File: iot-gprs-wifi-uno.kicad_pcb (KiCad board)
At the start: 2 copper layers, 110 x 53.3 mm, 73 parts, among them CON1 BARREL_JACK, P1 CAMERASOCKET, P2 CONN_01X12, P3 CONN_01X12, SW1 SW_DIP_x01, U1 usb_mini_b, U2 MCP16311-MNY, U3 CH340G, U4 A20Module, U5 MCP6001R, U6 IRLM6402, U7 BD00GA5WEFJ, U8 SIM, X1 CRYSTAL_ABM3C

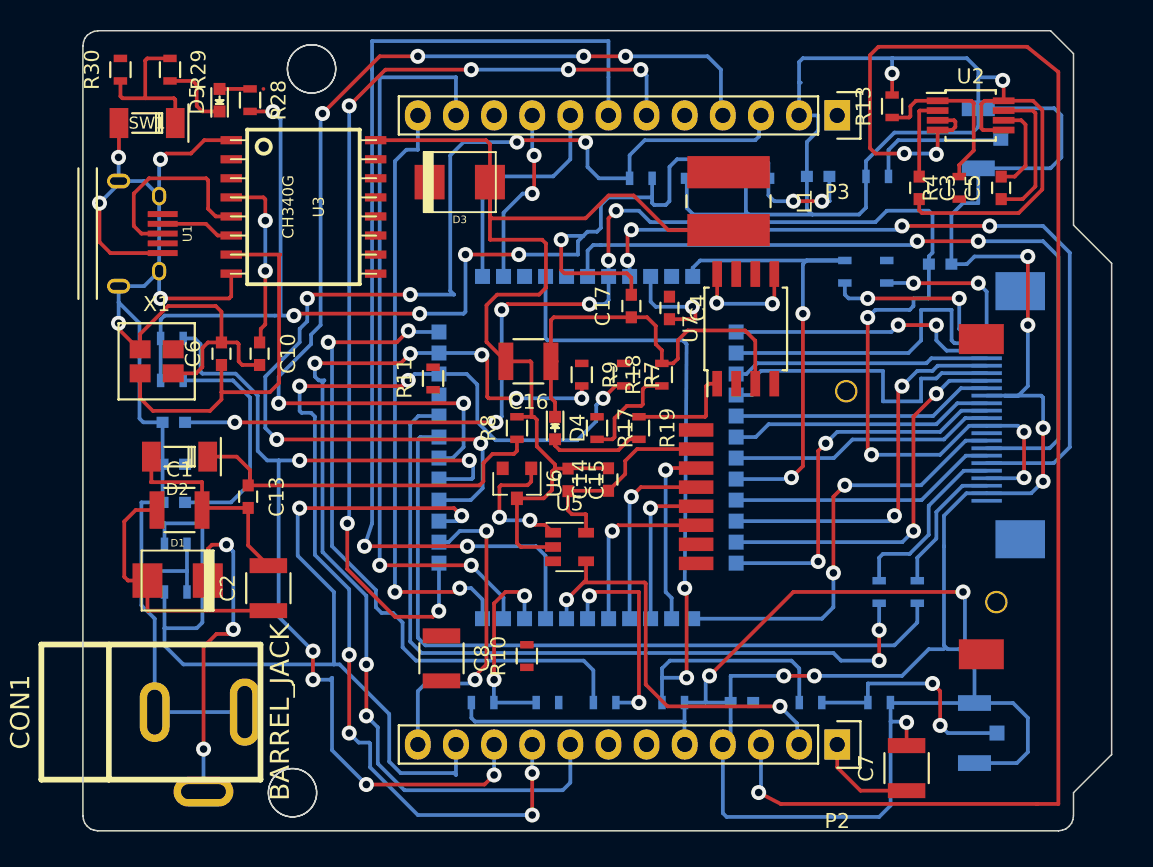
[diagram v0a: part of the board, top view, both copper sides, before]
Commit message: add .gitignore file add fp-lib-table
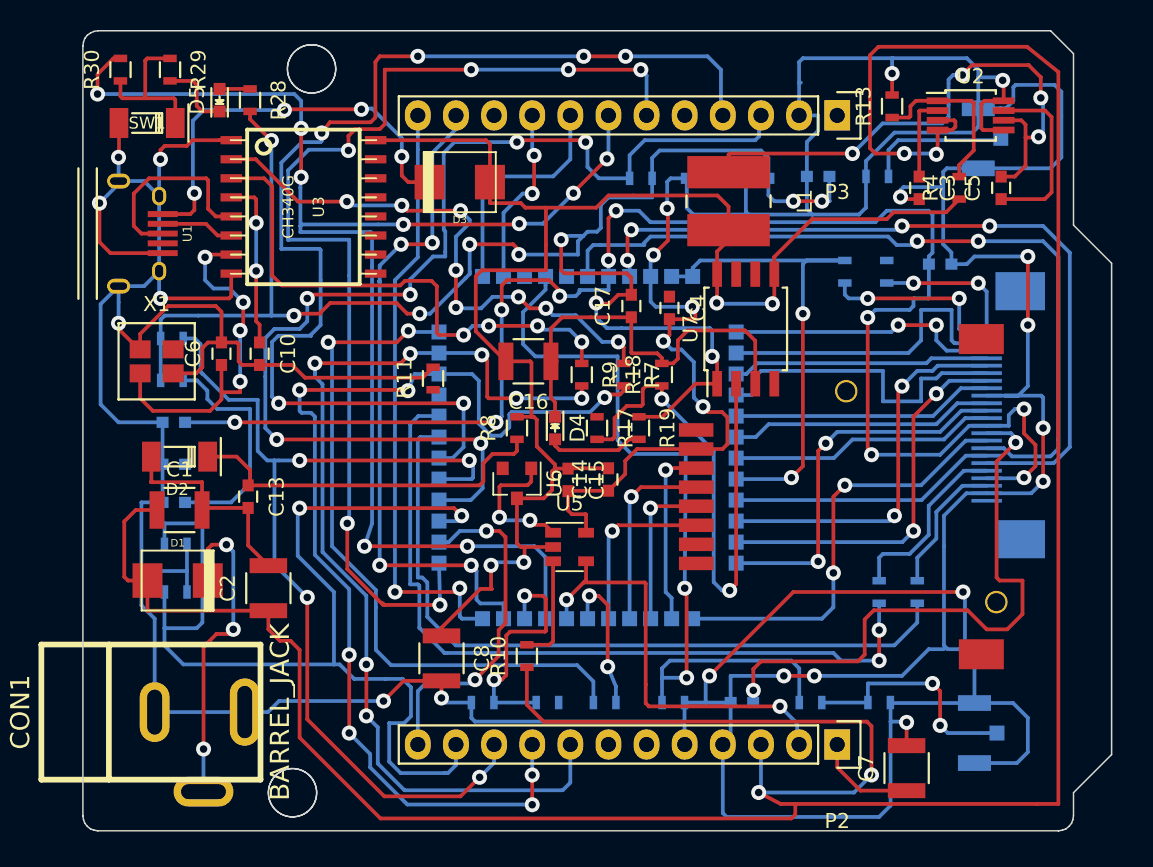
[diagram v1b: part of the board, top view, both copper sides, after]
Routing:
- net Vin: track 118.7 -> 201.8 mm, vias 3 -> 4
- net XO: track 401.5 -> 446.7 mm, vias 17 -> 24
- net VDD_1V8: track 0.00 -> 40.0 mm, vias 0 -> 2
- net Net-(R7-Pad1): track 0.00 -> 37.8 mm, vias 0 -> 8
- net Net-(R9-Pad1): track 0.00 -> 35.4 mm, vias 0 -> 4
- net Net-(C5-Pad2): track 6.24 -> 37.5 mm, vias 0 -> 4
- net Net-(R17-Pad2): track 7.13 -> 36.9 mm, vias 0 -> 2
- net VCC_USB: track 0.00 -> 27.8 mm, vias 0 -> 4
- net VCC5.0: track 87.5 -> 111.7 mm, vias 2 -> 4
- net WIFI_RST: track 71.0 -> 93.2 mm, vias 2 -> 9
- net VCC3.3: track 124.0 -> 137.3 mm, vias 10 -> 12
- net WIFI_IO12: track 65.3 -> 73.2 mm
- net WIFI_IO4: track 69.3 -> 76.8 mm
- net Net-(R10-Pad2): track 0.00 -> 7.17 mm
- net WIFI_TXD: track 50.7 -> 44.8 mm, vias 2 -> 4
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
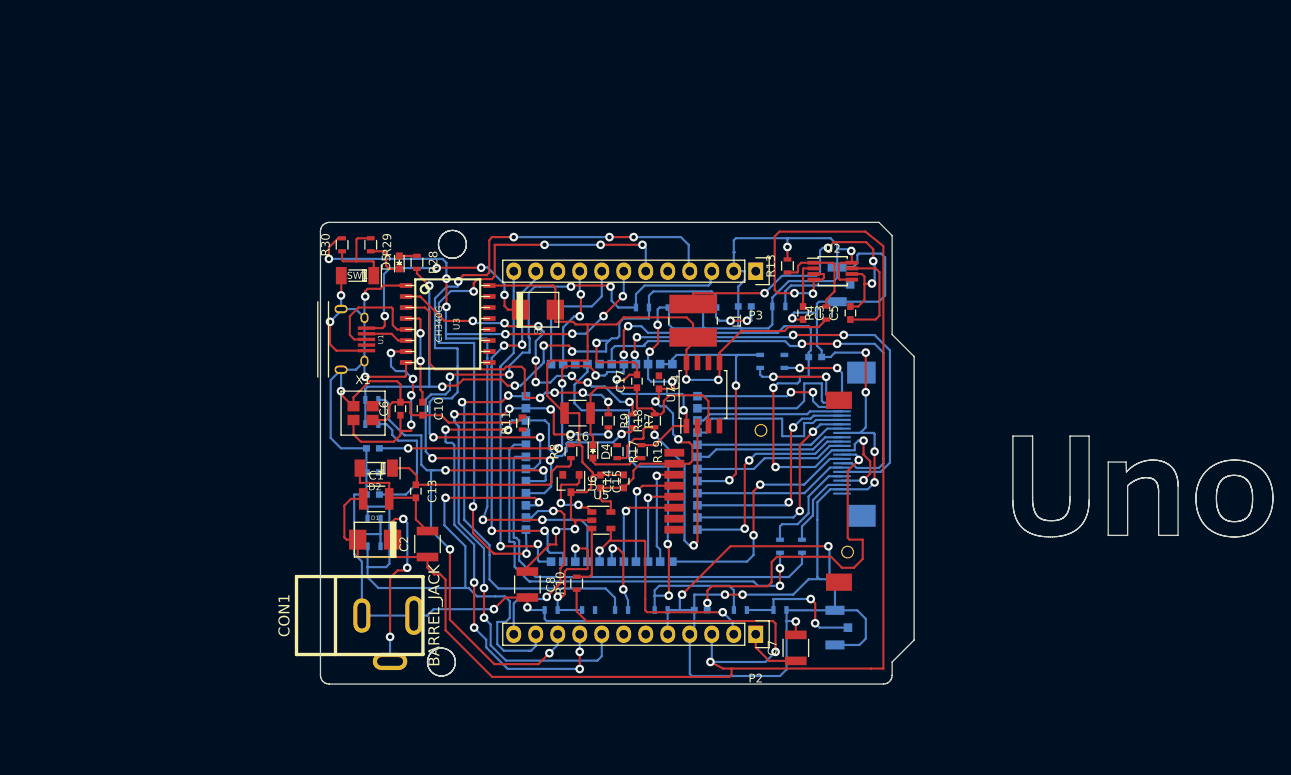
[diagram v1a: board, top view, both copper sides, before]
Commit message: update Kicad PCb iot-gprs-wifi-uno-hw
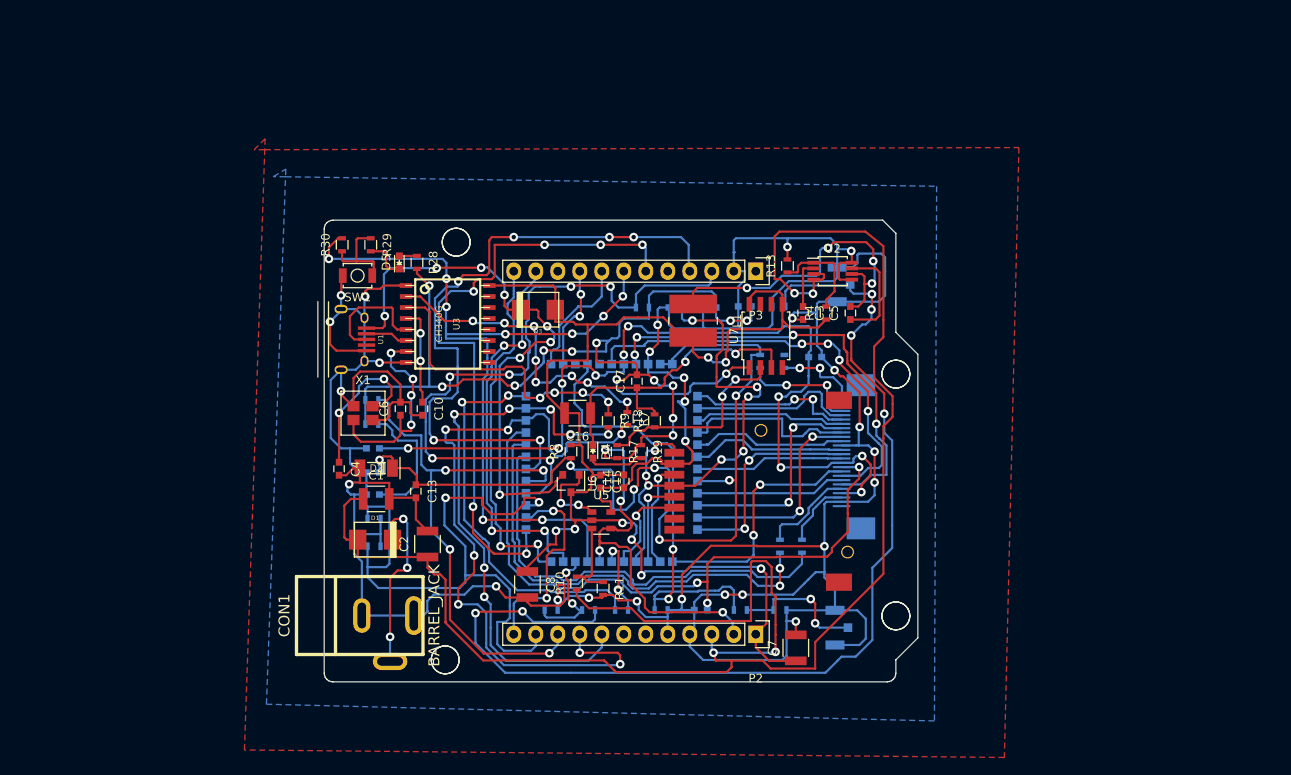
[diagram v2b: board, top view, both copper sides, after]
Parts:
- CON1: footprint A20md:dc_socket -> Footprint:dc_socket
- D1, D3: footprint A20md:do214aa -> Footprint:do214aa
- D2: footprint A20md:SOD-80 -> Footprint:SOD-80
- P1: footprint A20md:camera_socket24aaa -> Footprint:camera_socket24aaa
- SMA1, SMA2: footprint A20md:ANTEN_FP -> Footprint:ANTEN_FP
- SW1: value SW_DIP_x01 -> SW_PUSH; footprint A20md:SOD-80 -> Buttons_Switches_SMD:SW_SPST_B3U-1000P
- U1: footprint A20md:USB_Micro-B -> Footprint:USB_Micro-B
- U3: footprint A20md:soic-16 -> Footprint:soic-16
- U4: footprint A20md:a20module -> Footprint:a20module
- U8: footprint A20md:SIM_HOLD_115A-ADA0-R02 -> Footprint:SIM_HOLD_115A-ADA0-R02
- X1: footprint A20md:Crystal_SMD_3225_12MHz -> Footprint:Crystal_SMD_3225_12MHz
- moved C4 38.3 mm to (127.2, 114.5)
- moved R11 21.2 mm to (157.6, 128.3), turned to 270 degrees
- moved U7 9.92 mm to (176.4, 99.2)
- moved P1 1.45 mm to (188.4, 112.1)
- moved R7 0.66 mm to (160.4, 108.7)
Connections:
- R1 pad 1: XO -> Net-(R1-Pad1)
- R1 pad 2: Net-(R1-Pad2) -> XO
- R17 pad 1: VCC3.3 -> Net-(R17-Pad1)
- R17 pad 2: Net-(R17-Pad2) -> VCC3.3
- R18 pad 1: Net-(R17-Pad2) -> Net-(R17-Pad1)
- R2 pad 2: Net-(R1-Pad2) -> Net-(R1-Pad1)
- U4 pad 21: Net-(R1-Pad2) -> Net-(R1-Pad1)
- U7 pad 2: Net-(R17-Pad2) -> Net-(R17-Pad1)
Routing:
- net Net-(R2-Pad1): track 9.57 -> 124.9 mm, vias 0 -> 6
- net VCC3.9: track 58.3 -> 107.9 mm, vias 2 -> 7
- net VSIM: track 12.8 -> 58.9 mm, vias 1 -> 8
- net VCC5.0: track 111.7 -> 150.5 mm, vias 4 -> 8
- net VCC_USB: track 27.8 -> 64.7 mm, vias 4 -> 8
- net Net-(R17-Pad2): track 36.9 -> 0.00 mm, vias 2 -> 0
- net VDD_1V8: track 40.0 -> 75.8 mm, vias 2 -> 3
- net VCC3.3: track 137.3 -> 171.8 mm, vias 12 -> 18
- net Net-(R17-Pad1): track 0.00 -> 23.5 mm, vias 0 -> 2
- net Net-(C4-Pad1): track 0.00 -> 17.9 mm, vias 0 -> 2
- net Net-(R1-Pad2): track 15.9 -> 0.00 mm, vias 2 -> 0
- net Net-(R1-Pad1): track 0.00 -> 12.7 mm, vias 0 -> 2
- net UART_RXD: track 71.1 -> 83.1 mm
- net XO: track 446.7 -> 436.2 mm, vias 24 -> 27
- net Net-(C16-Pad1): track 28.0 -> 37.5 mm, vias 0 -> 2
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- added copper zone on B.Cu, net XO
- added copper zone on F.Cu, net XO
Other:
- board size 110 x 53.3 mm -> 68.5 x 53.3 mm

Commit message: update schematic iot-gprs-wifi-uno-hw add a20 pretty folder
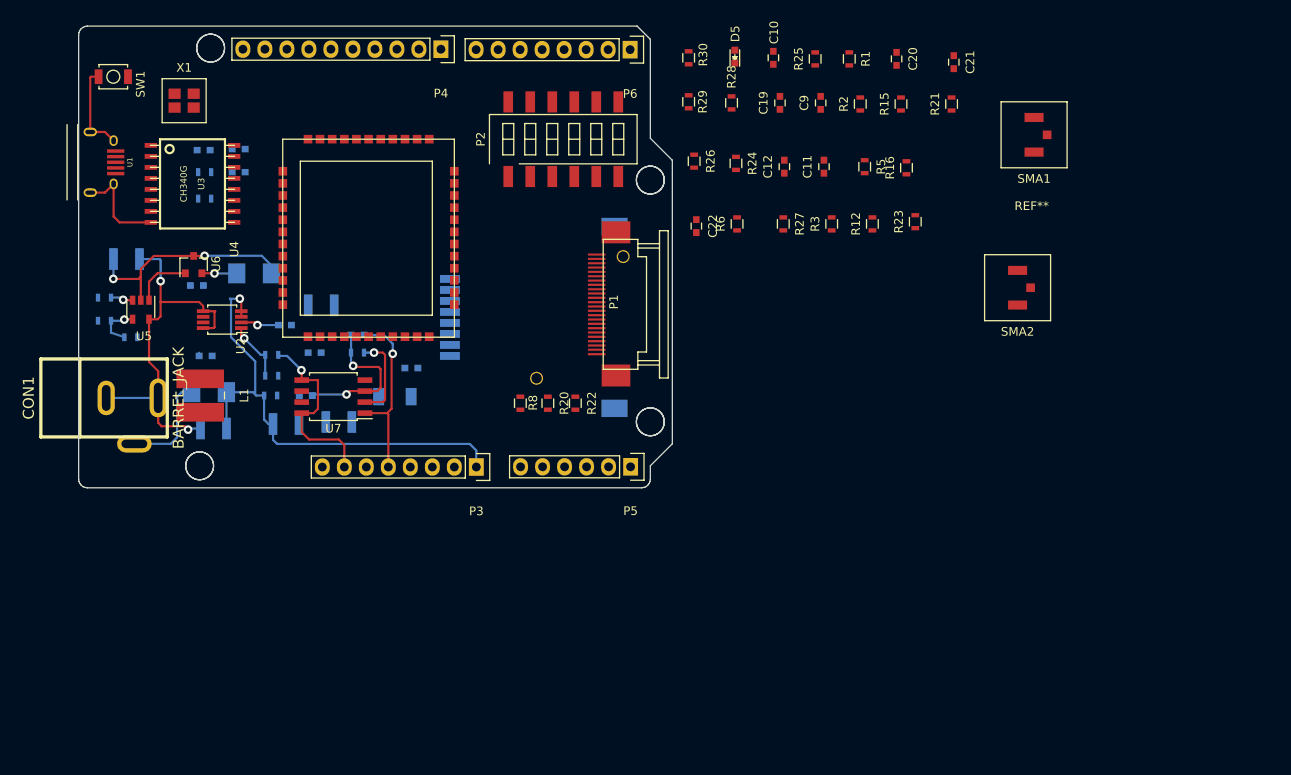
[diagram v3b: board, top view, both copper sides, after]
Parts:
- added Arduino_Header: Val**, A20:arduino_header, B.Cu at (68.2, 158.9)
- added P4: CONN_01X10, Socket_Strips:Socket_Strip_Straight_1x10, F.Cu at (138.9, 66.1)
- added P5: CONN_01X06, Socket_Strips:Socket_Strip_Straight_1x06, F.Cu at (160.8, 114.3)
- added P6: CONN_01X08, Socket_Strips:Socket_Strip_Straight_1x08, F.Cu at (160.8, 66.1)
- added REF**: esp8266.vn, A20:logo-esp8266.vn, F.Cu at (207.1, 83.7)
- C1, C13, C14, C15, C16, C17, C2, C3, C4, C5, C6, C7, C8, D4, R10, R11, R13, R17, R18, R19, R4, R7, R9: moved to B.Cu
- C11, C12, C19, C20, C21, C22, C9, R1, R12, R15, R16, R2, R20, R21, R22, R23, R24, R25, R26, R27, R3, R5, R6: moved to F.Cu
- CON1: footprint Footprint:dc_socket -> A20:dc_socket
- D1, D3: footprint Footprint:do214aa -> A20:do214aa; moved to B.Cu
- D2: footprint Footprint:SOD-80 -> A20:SOD-80; moved to B.Cu
- P1: footprint Footprint:camera_socket24aaa -> A20:camera_socket24aaa; moved to F.Cu
- P2: value CONN_01X12 -> SW2x6; footprint Socket_Strips:Socket_Strip_Straight_1x12 -> Buttons_Switches_ThroughHole:SW_DIP_x6_W8.61mm_Slide_SMD_LowProfile
- P3: value CONN_01X12 -> CONN_01X08; footprint Socket_Strips:Socket_Strip_Straight_1x12 -> Socket_Strips:Socket_Strip_Straight_1x08
- SMA1, SMA2: footprint Footprint:ANTEN_FP -> A20:ANTEN_FP; moved to F.Cu
- U1: footprint Footprint:USB_Micro-B -> A20:USB_Micro-B
- U3: footprint Footprint:soic-16 -> A20:soic-16
- U4: footprint Footprint:a20module -> A20:a20module; moved to F.Cu
- U8: footprint Footprint:SIM_HOLD_115A-ADA0-R02 -> A20:SIM_HOLD_115A-ADA0-R02; moved to B.Cu
- X1: footprint Footprint:Crystal_SMD_3225_12MHz -> A20:Crystal_SMD_3225_12MHz
- moved C5 74.6 mm to (111.8, 101.5), turned to 180 degrees
- moved R1 72.3 mm to (186.1, 67.2), turned to 270 degrees
- moved U2 70.7 mm to (113.7, 97.3), turned to 180 degrees
- moved C20 67.5 mm to (191.5, 67.2), turned to 270 degrees
- moved R11 66.6 mm to (100.1, 94.7), turned to 180 degrees
- moved R2 66.3 mm to (187.3, 72.4), turned to 90 degrees
- moved R4 64.2 mm to (119.4, 101.3), turned to 180 degrees
- moved C19 61.6 mm to (178.1, 72.3), turned to 90 degrees
- moved P2 61.3 mm to (153.0, 76.5), turned to 90 degrees
- moved R15 61.3 mm to (192.0, 72.4), turned to 90 degrees
- moved R17 61.1 mm to (100.1, 97.4), turned to 0 degrees
- moved R13 60.9 mm to (119.4, 103.8), turned to 0 degrees
- moved R19 60.4 mm to (103.1, 99.3), turned to 0 degrees
- moved R27 60.1 mm to (178.4, 86.2), turned to 270 degrees
- moved C3 59.8 mm to (120.9, 97.9), turned to 0 degrees
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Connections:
- net Net-(P2-Pad6) renamed WF_IO13
- P2 pad 1: VCC5.0 -> UART_RXD
- P2 pad 10: WIFI_IO0 -> U_TXD
- P2 pad 12: WIFI_IO13 -> U_RXD
- P2 pad 2: VCC3.3 -> UART_RXD
- P2 pad 3: Vin -> UART_TXD
- P2 pad 4: XO -> UART_TXD
- P2 pad 5: XO -> WF_IO15
- P2 pad 7: Net-(P2-Pad7) -> WIFI_IO13
- P2 pad 8: UART_TXD -> WIFI_IO15
- P2 pad 9: UART_RXD -> WIFI_IO13
- P3 pad 1: Net-(P3-Pad1) -> Vin
- P3 pad 3: WIFI_IO2 -> XO
- P3 pad 4: WIFI_IO4 -> VCC5.0
- P3 pad 5: Net-(P3-Pad5) -> VCC3.3
- P3 pad 6: WIFI_IO12 -> WIFI_IO13
- P3 pad 7: WIFI_RST -> VCC5.0
- P3 pad 8: HST_TXD -> Net-(P3-Pad8)
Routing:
- net XO: track 436.2 -> 66.3 mm, vias 27 -> 2
- net Vin: track 208.6 -> 56.2 mm, vias 4 -> 1
- net VCC3.3: track 171.8 -> 26.4 mm, vias 18 -> 2
- net Net-(R2-Pad1): track 124.9 -> 0.00 mm, vias 6 -> 0
- net VCC3.9: track 107.9 -> 0.00 mm, vias 7 -> 0
- net VCC5.0: track 150.5 -> 48.4 mm, vias 8 -> 3
- net VDD_2V8: track 101.9 -> 0.00 mm, vias 10 -> 0
- net WIFI_RST: track 93.4 -> 0.00 mm, vias 9 -> 0
- net UART_RXD: track 83.1 -> 0.00 mm, vias 7 -> 0
- net WIFI_IO2: track 76.9 -> 0.00 mm, vias 6 -> 0
- net WIFI_IO4: track 76.8 -> 0.00 mm, vias 6 -> 0
- net VDD_1V8: track 75.8 -> 0.00 mm, vias 3 -> 0
- net WIFI_IO15: track 74.5 -> 0.00 mm, vias 2 -> 0
- net WIFI_IO12: track 73.2 -> 0.00 mm, vias 6 -> 0
- net UART_TXD: track 66.6 -> 0.00 mm, vias 7 -> 0
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- removed copper zone on B.Cu, net XO
- removed copper zone on F.Cu, net XO
